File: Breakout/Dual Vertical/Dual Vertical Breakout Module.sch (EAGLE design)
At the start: 4 parts

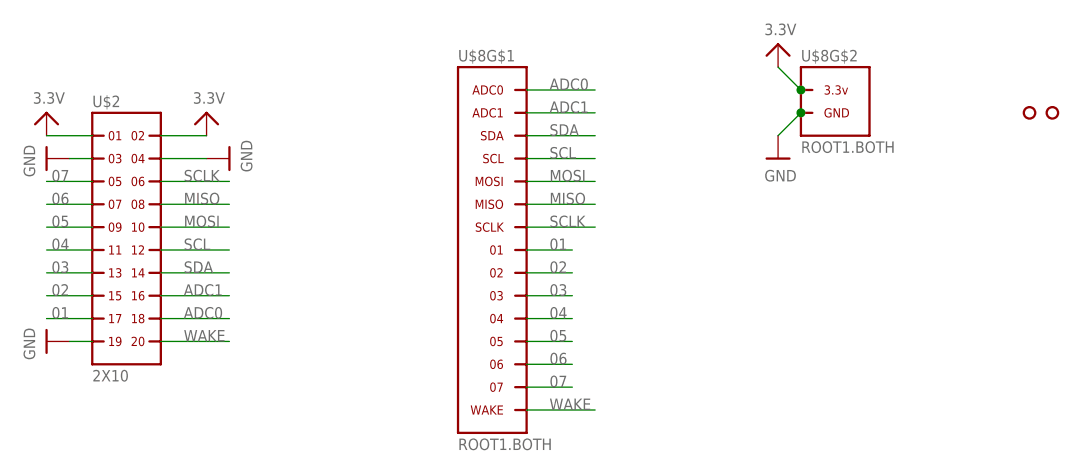
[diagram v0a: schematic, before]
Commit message: Updated Root1 connector labels. Renamed Dual Horizontal Breakout Module. Both breakout files need silkscreen.
Signed-off-by: Cruz Monrreal II <Cruz.Monrreal@gmail.com>
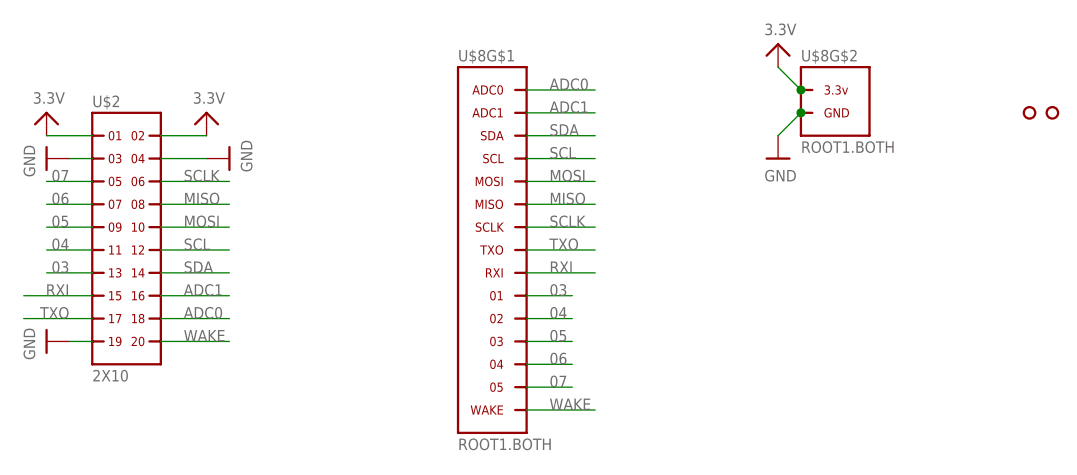
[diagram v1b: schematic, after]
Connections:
- removed net 01: U$2.17, U$8G$1.01
- removed net 02: U$2.15, U$8G$1.02
- new net RXI: U$2.15, U$8G$1.RXI
- new net TXO: U$2.17, U$8G$1.TXO
- net 03: now also U$8G$1.01; no longer U$8G$1.03
- net 04: now also U$8G$1.02; no longer U$8G$1.04
- net 05: now also U$8G$1.03; no longer U$8G$1.05
- net 06: now also U$8G$1.04; no longer U$8G$1.06
- net 07: now also U$8G$1.05; no longer U$8G$1.07
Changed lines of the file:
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@@
 <grid distance="0.1" unitdist="inch" unit="inch" style="lines" multiple="1" display="no" altdistance="0.01" altunitdist="inch" altunit="inch"/>
 <layers>
-<layer number="1" name="Top" color="4" fill="1" visible="yes" active="no"/>
-<layer number="16" name="Bottom" color="1" fill="1" visible="yes" active="no"/>
-<layer number="17" name="Pads" color="2" fill="1" visible="yes" active="no"/>
-<layer number="18" name="Vias" color="2" fill="1" visible="yes" active="no"/>
-<layer number="19" name="Unrouted" color="6" fill="1" visible="yes" active="no"/>
-<layer number="20" name="Dimension" color="15" fill="1" visible="yes" active="no"/>
-<layer number="21" name="tPlace" color="7" fill="1" visible="yes" active="no"/>
-<layer number="22" name="bPlace" color="7" fill="1" visible="yes" active="no"/>
-<layer number="23" name="tOrigins" color="15" fill="1" visible="yes" active="no"/>
-<layer number="24" name="bOrigins" color="15" fill="1" visible="yes" active="no"/>
-<layer number="25" name="tNames" color="7" fill="1" visible="yes" active="no"/>
-<layer number="26" name="bNames" color="7" fill="1" visible="yes" active="no"/>
-<layer number="27" name="tValues" color="7" fill="1" visible="yes" active="no"/>
-<layer number="28" name="bValues" color="7" fill="1" visible="yes" active="no"/>
+<layer number="1" name="Top" color="4" fill="1" visible="no" active="no"/>
+<layer number="16" name="Bottom" color="1" fill="1" visible="no" active="no"/>
+<layer number="17" name="Pads" color="2" fill="1" visible="no" active="no"/>
+<layer number="18" name="Vias" color="2" fill="1" visible="no" active="no"/>
+<layer number="19" name="Unrouted" color="6" fill="1" visible="no" active="no"/>
+<layer number="20" name="Dimension" color="15" fill="1" visible="no" active="no"/>
+<layer number="21" name="tPlace" color="7" fill="1" visible="no" active="no"/>
+<layer number="22" name="bPlace" color="7" fill="1" visible="no" active="no"/>
+<layer number="23" name="tOrigins" color="15" fill="1" visible="no" active="no"/>
+<layer number="24" name="bOrigins" color="15" fill="1" visible="no" active="no"/>
+<layer number="25" name="tNames" color="7" fill="1" visible="no" active="no"/>
+<layer number="26" name="bNames" color="7" fill="1" visible="no" active="no"/>
+<layer number="27" name="tValues" color="7" fill="1" visible="no" active="no"/>
+<layer number="28" name="bValues" color="7" fill="1" visible="no" active="no"/>
 <layer number="29" name="tStop" color="7" fill="3" visible="no" active="no"/>
 <layer number="30" name="bStop" color="7" fill="6" visible="no" active="no"/>
@@
 <layer number="35" name="tGlue" color="7" fill="4" visible="no" active="no"/>
 <layer number="36" name="bGlue" color="7" fill="5" visible="no" active="no"/>
-<layer number="37" name="tTest" color="7" fill="1" visible="yes" active="no"/>
-<layer number="38" name="bTest" color="7" fill="1" visible="yes" active="no"/>
+<layer number="37" name="tTest" color="7" fill="1" visible="no" active="no"/>
+<layer number="38" name="bTest" color="7" fill="1" visible="no" active="no"/>
 <layer number="39" name="tKeepout" color="4" fill="11" visible="no" active="no"/>
 <layer number="40" name="bKeepout" color="1" fill="11" visible="no" active="no"/>
@@
 <layer number="44" name="Drills" color="7" fill="1" visible="no" active="no"/>
 <layer number="45" name="Holes" color="7" fill="1" visible="no" active="no"/>
-<layer number="46" name="Milling" color="3" fill="1" visible="yes" active="no"/>
-<layer number="47" name="Measures" color="7" fill="1" visible="yes" active="no"/>
-<layer number="48" name="Document" color="7" fill="1" visible="yes" active="no"/>
-<layer number="49" name="Reference" color="7" fill="1" visible="yes" active="no"/>
-<layer number="50" name="dxf" color="7" fill="1" visible="yes" active="no"/>
-<layer number="51" name="tDocu" color="7" fill="1" visible="yes" active="no"/>
-<layer number="52" name="bDocu" color="7" fill="1" visible="yes" active="no"/>
-<layer number="53" name="tGND_GNDA" color="7" fill="9" visible="yes" active="no"/>
-<layer number="54" name="bGND_GNDA" color="1" fill="9" visible="yes" active="no"/>
-<layer number="56" name="wert" color="7" fill="1" visible="yes" active="no"/>
+<layer number="46" name="Milling" color="3" fill="1" visible="no" active="no"/>
+<layer number="47" name="Measures" color="7" fill="1" visible="no" active="no"/>
+<layer number="48" name="Document" color="7" fill="1" visible="no" active="no"/>
+<layer number="49" name="Reference" color="7" fill="1" visible="no" active="no"/>
+<layer number="50" name="dxf" color="7" fill="1" visible="no" active="no"/>
+<layer number="51" name="tDocu" color="7" fill="1" visible="no" active="no"/>
+<layer number="52" name="bDocu" color="7" fill="1" visible="no" active="no"/>
+<layer number="53" name="tGND_GNDA" color="7" fill="9" visible="no" active="no"/>
+<layer number="54" name="bGND_GNDA" color="1" fill="9" visible="no" active="no"/>
+<layer number="56" name="wert" color="7" fill="1" visible="no" active="no"/>
 <layer number="91" name="Nets" color="2" fill="1" visible="yes" active="yes"/>
 <layer number="92" name="Busses" color="1" fill="1" visible="yes" active="yes"/>
@@
 </segment>
 </net>
-<net name="01" class="0">
+<net name="TXO" class="0">
+<segment>
+<pinref part="U$8" gate="G$1" pin="TXO"/>
+<wire x1="182.88" y1="111.76" x2="175.26" y2="111.76" width="0.1524" layer="91"/>
+<label x="177.8" y="111.76" size="1.27" layer="95"/>
+</segment>
+<segment>
+<pinref part="U$2" gate="G$1" pin="17"/>
+<wire x1="127" y1="104.14" x2="119.38" y2="104.14" width="0.1524" layer="91"/>
+<label x="124.46" y="104.14" size="1.27" layer="95" rot="MR0"/>
+</segment>
+</net>
+<net name="RXI" class="0">
+<segment>
+<pinref part="U$8" gate="G$1" pin="RXI"/>
+<wire x1="175.26" y1="109.22" x2="182.88" y2="109.22" width="0.1524" layer="91"/>
+<label x="177.8" y="109.22" size="1.27" layer="95"/>
+</segment>
+<segment>
+<pinref part="U$2" gate="G$1" pin="15"/>
+<wire x1="119.38" y1="106.68" x2="127" y2="106.68" width="0.1524" layer="91"/>
+<label x="124.46" y="106.68" size="1.27" layer="95" rot="MR0"/>
+</segment>
+</net>
+<net name="03" class="0">
 <segment>
 <pinref part="U$8" gate="G$1" pin="01"/>
-<wire x1="180.34" y1="111.76" x2="175.26" y2="111.76" width="0.1524" layer="91"/>
-<label x="177.8" y="111.76" size="1.27" layer="95"/>
-</segment>
-<segment>
-<pinref part="U$2" gate="G$1" pin="17"/>
-<wire x1="127" y1="104.14" x2="121.92" y2="104.14" width="0.1524" layer="91"/>
-<label x="124.46" y="104.14" size="1.27" layer="95" rot="MR0"/>
-</segment>
-</net>
-<net name="02" class="0">
-<segment>
-<pinref part="U$8" gate="G$1" pin="02"/>
-<wire x1="175.26" y1="109.22" x2="180.34" y2="109.22" width="0.1524" layer="91"/>
-<label x="177.8" y="109.22" size="1.27" layer="95"/>
-</segment>
-<segment>
-<pinref part="U$2" gate="G$1" pin="15"/>
-<wire x1="121.92" y1="106.68" x2="127" y2="106.68" width="0.1524" layer="91"/>
-<label x="124.46" y="106.68" size="1.27" layer="95" rot="MR0"/>
-</segment>
-</net>
-<net name="03" class="0">
-<segment>
-<pinref part="U$8" gate="G$1" pin="03"/>
 <wire x1="180.34" y1="106.68" x2="175.26" y2="106.68" width="0.1524" layer="91"/>
 <label x="177.8" y="106.68" size="1.27" layer="95"/>
@@
 <net name="04" class="0">
 <segment>
-<pinref part="U$8" gate="G$1" pin="04"/>
+<pinref part="U$8" gate="G$1" pin="02"/>
 <wire x1="175.26" y1="104.14" x2="180.34" y2="104.14" width="0.1524" layer="91"/>
 <label x="177.8" y="104.14" size="1.27" layer="95"/>
@@
 <net name="05" class="0">
 <segment>
-<pinref part="U$8" gate="G$1" pin="05"/>
+<pinref part="U$8" gate="G$1" pin="03"/>
 <wire x1="180.34" y1="101.6" x2="175.26" y2="101.6" width="0.1524" layer="91"/>
 <label x="177.8" y="101.6" size="1.27" layer="95"/>
@@
 <net name="06" class="0">
 <segment>
-<pinref part="U$8" gate="G$1" pin="06"/>
+<pinref part="U$8" gate="G$1" pin="04"/>
 <wire x1="175.26" y1="99.06" x2="180.34" y2="99.06" width="0.1524" layer="91"/>
 <label x="177.8" y="99.06" size="1.27" layer="95"/>
@@
 <net name="07" class="0">
 <segment>
-<pinref part="U$8" gate="G$1" pin="07"/>
+<pinref part="U$8" gate="G$1" pin="05"/>
 <wire x1="180.34" y1="96.52" x2="175.26" y2="96.52" width="0.1524" layer="91"/>
 <label x="177.8" y="96.52" size="1.27" layer="95"/>
